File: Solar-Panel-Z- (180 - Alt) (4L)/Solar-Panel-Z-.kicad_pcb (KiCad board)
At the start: 4 copper layers, 48.4 x 48.4 mm, 88 parts, among them J1 FTS-105-01-L-DV-A, J2 U.FL-R-SMT-1, Q1 BSS138DWQ-7, Q2 MBT2222ADW1T1, Q3 BSS138DWQ-7, Q4 MBT2222ADW1T1, Q5 IRLML2803, U1 BQ25570RGRR, U2 TSL2561, U3 ATB2012-50011-T000, U4 NDS8434

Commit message: New Y- and Z- boards
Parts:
- moved C6 2.21 mm to (112.1, 56.9), turned to 0 degrees
- moved U4 1.33 mm to (99.7, 79.4)
- moved R10 1.27 mm to (112.7, 59.5), turned to -90 degrees
- moved C10 1.09 mm to (110.9, 53.6)
- moved R33 1.00 mm to (95.2, 78.0)
- moved D2 0.96 mm to (105.5, 49.0)
- moved C11 0.96 mm to (102.8, 49.5)
- moved C8 0.92 mm to (110.9, 54.6)
- moved Q5 0.89 mm to (92.8, 77.5)
- moved R32 0.63 mm to (94.1, 80.0)
- moved R4 0.63 mm to (92.1, 80.0)
- moved R11 0.58 mm to (112.1, 57.9)
- moved R19 0.41 mm to (112.1, 55.9)
- moved D3 0.28 mm to (123.2, 61.8)
- moved D4 0.28 mm to (123.2, 57.2)
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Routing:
- net /VBURN: track 27.4 -> 0.00 mm, vias 5 -> 0
- net Net-(D3-Pad1): track 27.8 -> 17.1 mm
- net BATT_P: track 13.4 -> 4.50 mm, vias 4 -> 0
- net SCL_LS: track 70.1 -> 61.2 mm
- net SDA_LS: track 60.0 -> 53.6 mm
- net +3V3: track 31.0 -> 26.2 mm, vias 7 -> 8
- net GND: track 16.5 -> 19.1 mm, vias 4 -> 30
- net Net-(R10-Pad2): track 8.19 -> 6.32 mm
- net VBAT: track 61.8 -> 60.5 mm
- net /VSOLAR_FULL: track 47.1 -> 46.1 mm
- net Net-(C10-Pad1): track 3.99 -> 3.14 mm
- net Net-(Q5-Pad3): track 5.22 -> 4.67 mm
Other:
- board text added: "Rev B1/02"
- board text removed: "Rev B/02"

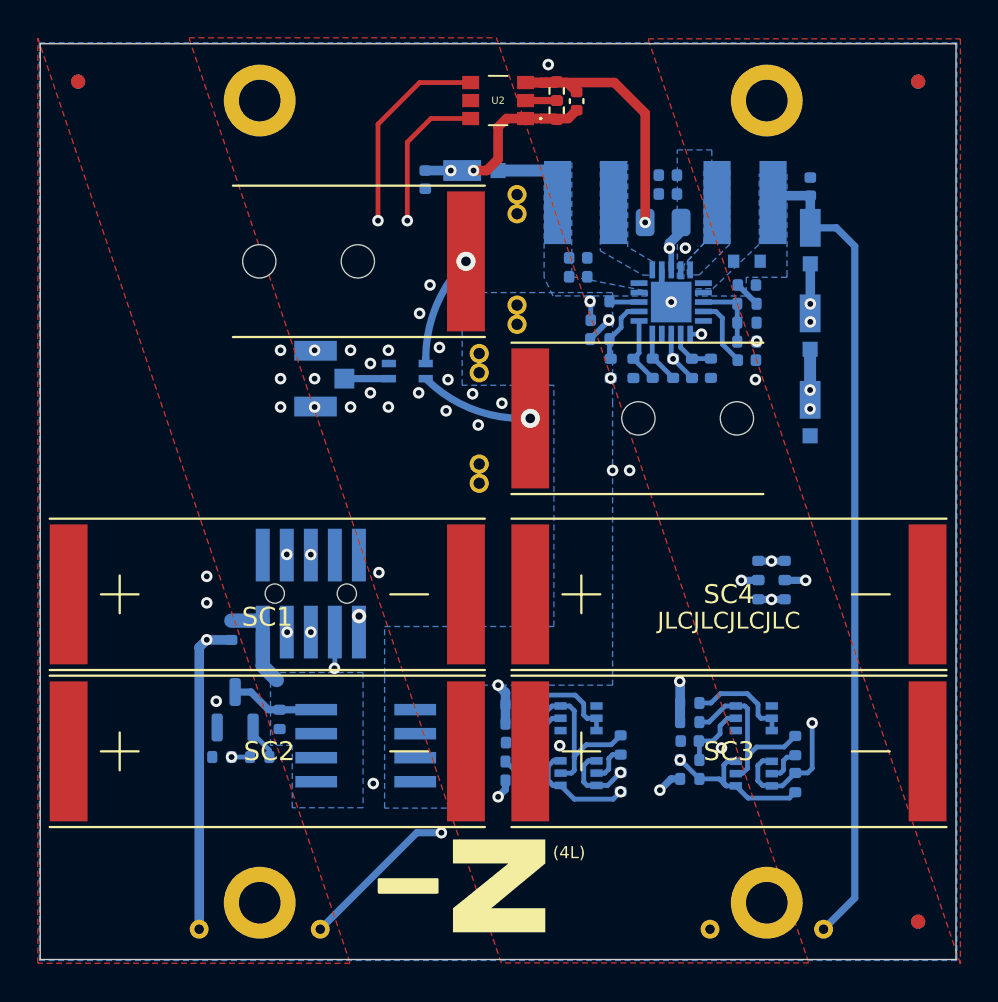
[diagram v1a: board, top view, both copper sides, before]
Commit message: Added antenna cable silkscreen lines
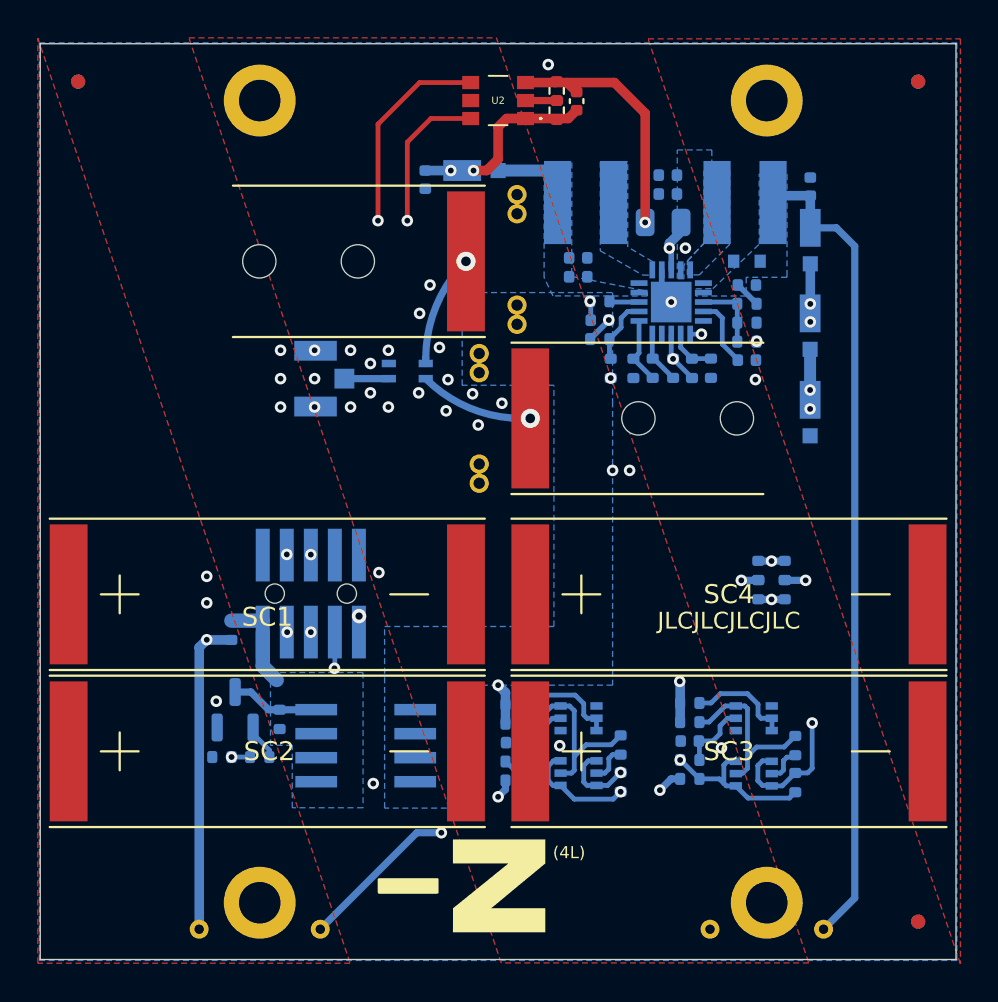
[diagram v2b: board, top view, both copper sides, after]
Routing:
- net /coil: track 5774.0 -> 5767.9 mm
- net GND: track 19.1 -> 16.2 mm
- net +3V3: track 26.2 -> 24.3 mm
- net Net-(D3-Pad1): track 17.1 -> 15.7 mm
